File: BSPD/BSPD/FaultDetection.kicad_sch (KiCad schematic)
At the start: 14 parts, among them U9 74HC32D_653

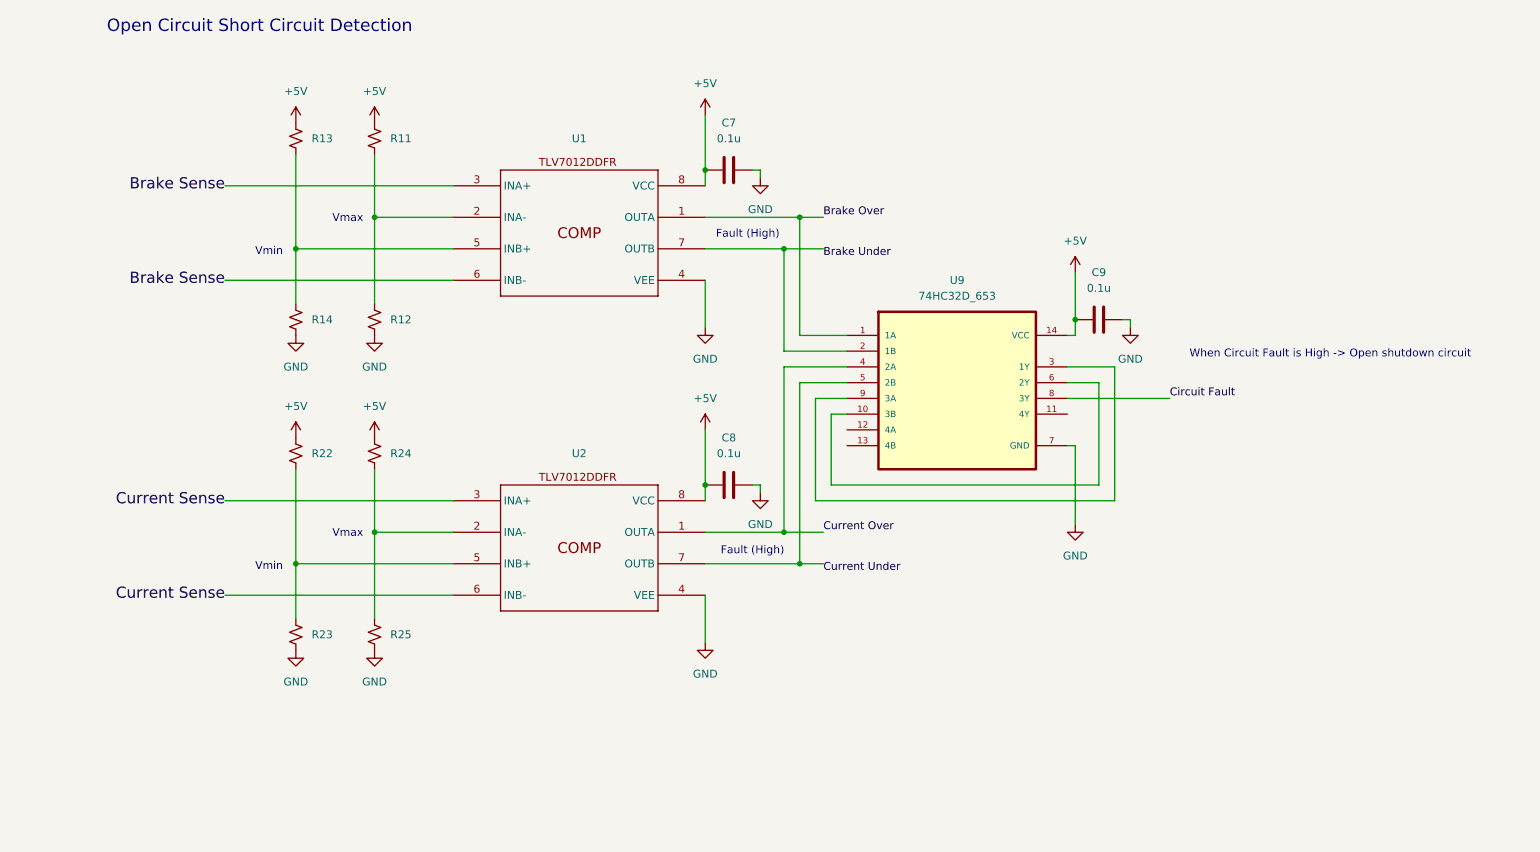
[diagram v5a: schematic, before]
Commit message: Layout started and component changes
The footprints have all be chosen and the linear regulator was swapped out.
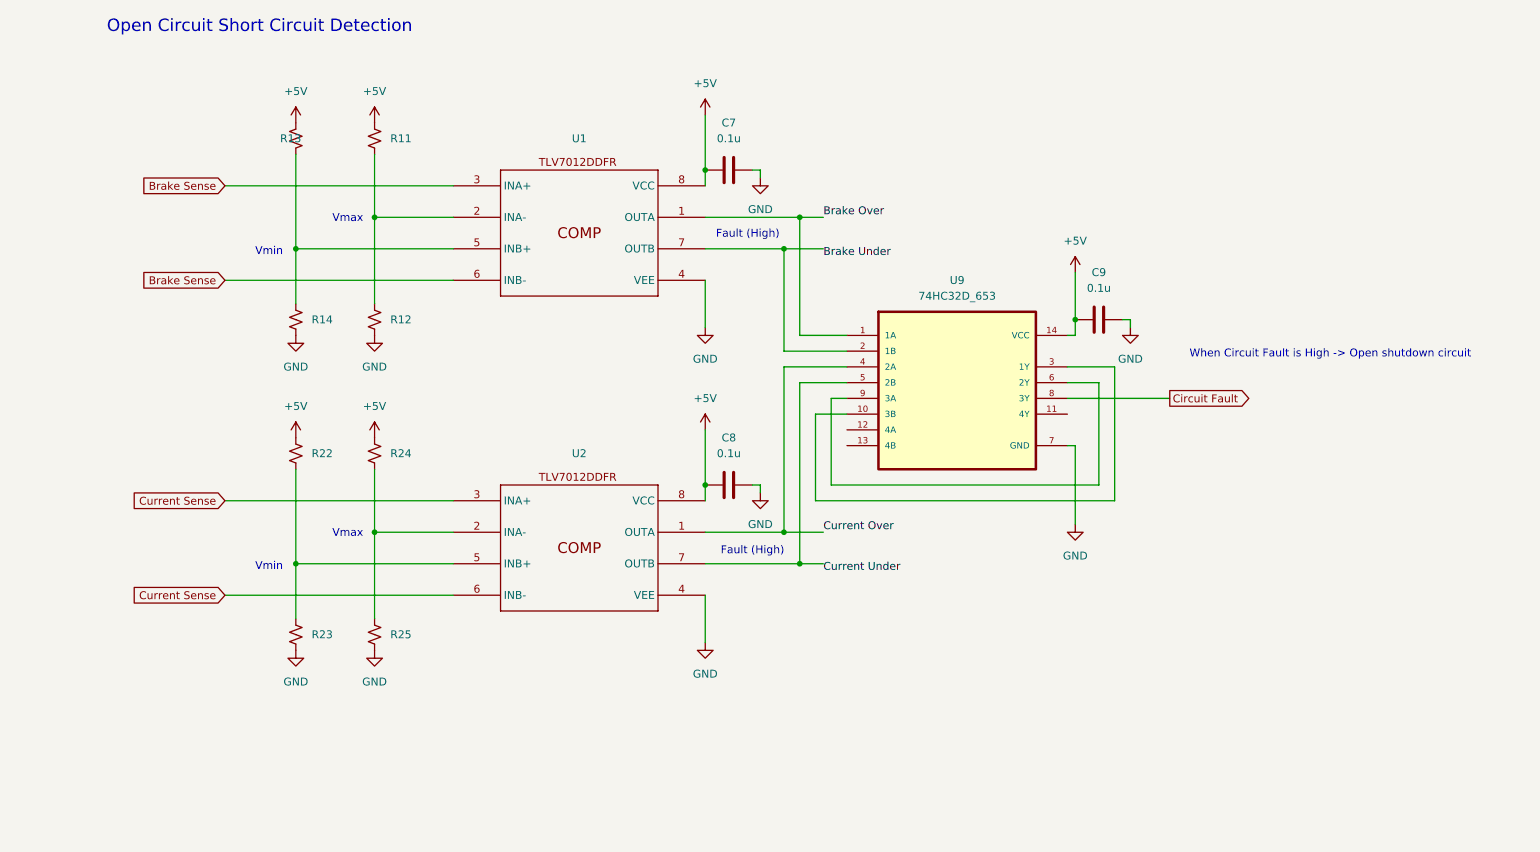
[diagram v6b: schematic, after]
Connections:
- net at U9.10 (3B): now also U9.3 (1Y); no longer U9.6 (2Y)
- net at U9.9 (3A): now also U9.6 (2Y); no longer U9.3 (1Y)
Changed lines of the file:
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@@
-	(wire
-		(pts
-			(xy 146.05 86.36) (xy 146.05 102.87)
-		)
-		(stroke
-			(width 0)
-			(type default)
-		)
-	)
 	(wire
 		(pts
@@
 	(wire
 		(pts
-			(xy 148.59 88.9) (xy 151.13 88.9)
+			(xy 148.59 86.36) (xy 151.13 86.36)
 		)
 		(stroke
@@
 	(wire
 		(pts
+			(xy 146.05 88.9) (xy 146.05 102.87)
+		)
+		(stroke
+			(width 0)
+			(type default)
+		)
+	)
+	(wire
+		(pts
 			(xy 191.77 83.82) (xy 191.77 100.33)
 		)
@@
 	(wire
 		(pts
+			(xy 148.59 86.36) (xy 148.59 100.33)
+		)
+		(stroke
+			(width 0)
+			(type default)
+		)
+	)
+	(wire
+		(pts
 			(xy 62.23 113.03) (xy 87.63 113.03)
 		)
@@
 	(wire
 		(pts
-			(xy 151.13 86.36) (xy 146.05 86.36)
+			(xy 151.13 88.9) (xy 146.05 88.9)
 		)
 		(stroke
@@
 		(pts
 			(xy 140.97 62.23) (xy 128.27 62.23)
-		)
-		(stroke
-			(width 0)
-			(type default)
-		)
-	)
-	(wire
-		(pts
-			(xy 148.59 100.33) (xy 148.59 88.9)
 		)
 		(stroke
@@
 		)
 	)
-	(label "Current Sense"
-		(at 50.8 102.87 180)
-		(fields_autoplaced yes)
-		(effects
-			(font
-				(size 1.8 1.8)
-			)
-			(justify right)
-		)
-	)
-	(label "Circuit Fault"
-		(at 203.2 86.36 0)
+	(label "Current Under"
+		(at 147.32 113.03 0)
 		(fields_autoplaced yes)
 		(effects
@@
 				(size 1.27 1.27)
 			)
-			(justify left bottom)
-		)
-	)
-	(label "Brake Sense"
-		(at 50.8 52.07 180)
-		(fields_autoplaced yes)
-		(effects
-			(font
-				(size 1.8 1.8)
-			)
-			(justify right)
-		)
-	)
-	(label "Current Sense"
-		(at 50.8 118.11 180)
-		(fields_autoplaced yes)
-		(effects
-			(font
-				(size 1.8 1.8)
-			)
-			(justify right)
-		)
-	)
-	(label "Current Under"
-		(at 147.32 113.03 0)
+			(justify left top)
+		)
+	)
+	(label "Current Over"
+		(at 147.32 107.95 0)
 		(fields_autoplaced yes)
 		(effects
@@
 				(size 1.27 1.27)
 			)
-			(justify left top)
-		)
-	)
-	(label "Current Over"
-		(at 147.32 107.95 0)
+			(justify left bottom)
+		)
+	)
+	(label "Brake Under"
+		(at 147.32 62.23 0)
 		(fields_autoplaced yes)
 		(effects
@@
 				(size 1.27 1.27)
 			)
-			(justify left bottom)
-		)
-	)
-	(label "Brake Under"
-		(at 147.32 62.23 0)
+			(justify left top)
+		)
+	)
+	(global_label "Circuit Fault"
+		(shape output)
+		(at 203.2 86.36 0)
 		(fields_autoplaced yes)
 		(effects
@@
 				(size 1.27 1.27)
 			)
-			(justify left top)
-		)
-	)
-	(label "Brake Sense"
+			(justify left)
+		)
+		(property "Intersheetrefs" "${INTERSHEET_REFS}"
+			(at 218.1594 86.36 0)
+			(effects
+				(font
+					(size 1.27 1.27)
+				)
+				(justify left)
+				(hide yes)
+			)
+		)
+	)
+	(global_label "Brake Sense"
+		(shape input)
 		(at 50.8 67.31 180)
 		(fields_autoplaced yes)
 		(effects
 			(font
-				(size 1.8 1.8)
+				(size 1.27 1.27)
 			)
 			(justify right)
+		)
+		(property "Intersheetrefs" "${INTERSHEET_REFS}"
+			(at 35.9615 67.31 0)
+			(effects
+				(font
+					(size 1.27 1.27)
+				)
+				(justify right)
+				(hide yes)
+			)
+		)
+	)
+	(global_label "Current Sense"
+		(shape input)
+		(at 50.8 102.87 180)
+		(fields_autoplaced yes)
+		(effects
+			(font
+				(size 1.27 1.27)
+			)
+			(justify right)
+		)
+		(property "Intersheetrefs" "${INTERSHEET_REFS}"
+			(at 34.3287 102.87 0)
+			(effects
+				(font
+					(size 1.27 1.27)
+				)
+				(justify right)
+				(hide yes)
+			)
+		)
+	)
+	(global_label "Current Sense"
+		(shape input)
+		(at 50.8 118.11 180)
+		(fields_autoplaced yes)
+		(effects
+			(font
+				(size 1.27 1.27)
+			)
+			(justify right)
+		)
+		(property "Intersheetrefs" "${INTERSHEET_REFS}"
+			(at 34.3287 118.11 0)
+			(effects
+				(font
+					(size 1.27 1.27)
+				)
+				(justify right)
+				(hide yes)
+			)
+		)
+	)
+	(global_label "Brake Sense"
+		(shape input)
+		(at 50.8 52.07 180)
+		(fields_autoplaced yes)
+		(effects
+			(font
+				(size 1.27 1.27)
+			)
+			(justify right)
+		)
+		(property "Intersheetrefs" "${INTERSHEET_REFS}"
+			(at 35.9615 52.07 0)
+			(effects
+				(font
+					(size 1.27 1.27)
+				)
+				(justify right)
+				(hide yes)
+			)
 		)
 	)
@@
 		(lib_id "Device:R_Small_US")
 		(at 62.23 44.45 0)
+		(mirror y)
 		(unit 1)
 		(exclude_from_sim no)
@@
 		(on_board yes)
 		(dnp no)
-		(fields_autoplaced yes)
 		(property "Reference" "R13"
-			(at 64.77 44.4499 0)
-			(effects
-				(font
-					(size 1.27 1.27)
-				)
-				(justify left)
+			(at 59.69 44.4499 0)
+			(effects
+				(font
+					(size 1.27 1.27)
+				)
+				(justify right)
 			)
 		)
 		(property "Value" "R_Small_US"
-			(at 64.77 45.7199 0)
-			(effects
-				(font
+			(at 59.69 45.7199 0)
+			(effects
+				(font
